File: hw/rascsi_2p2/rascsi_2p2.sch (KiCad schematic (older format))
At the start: 90 parts, among them IC1 SN74LS641-1DW, IC2 SN74LS641-1DW, IC3 SN74LS641-1DW, IC4 SN74LS641-1DW, J1 Raspberry_Pi_2_3, J2 Conn_01x02_Male, J3 Conn_02x25_Odd_Even, J4 I2C Pinout, J5 Conn_02x03_Odd_Even, J6 L717SDB25PA4CH4F, J7 Conn_01x02_Male, X1 Mac, X2 Dogcow, X3 Mac2, X4 Raspberry Pi, X5 Dogcow2, X6 Mac Trashcan, X7 Pi, X8 Pi

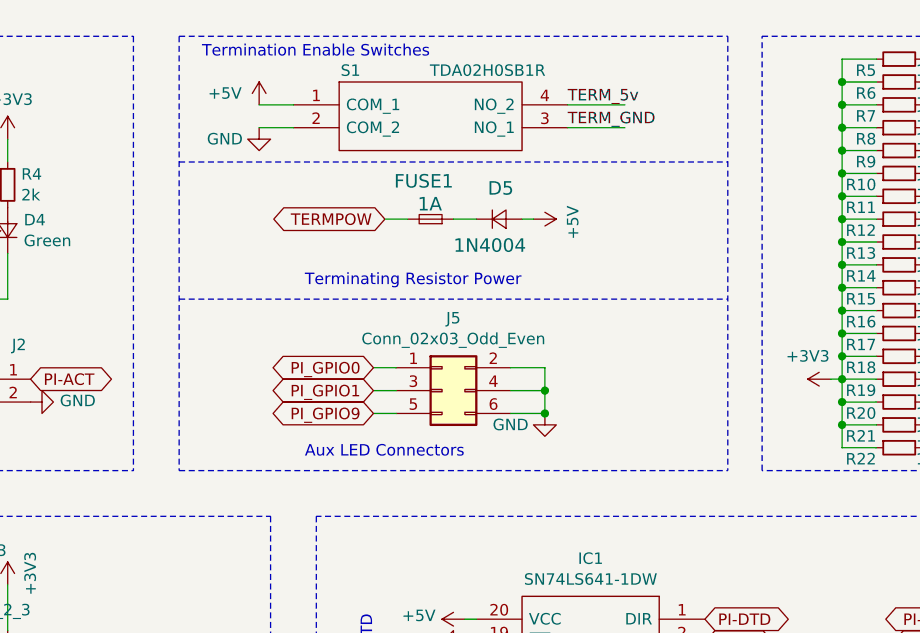
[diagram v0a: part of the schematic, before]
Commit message: Added USB port to power the raspberry pi. Labeled more pins on the silkscreen
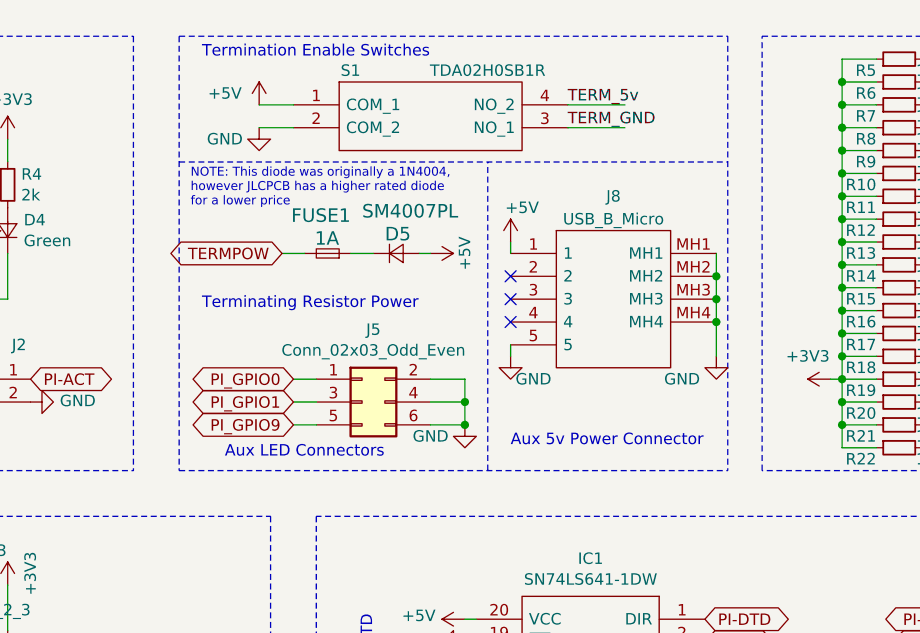
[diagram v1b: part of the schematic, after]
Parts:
- added J8: USB_B_Micro, SamacSys_Parts:U254051N4BH806, symbol SamacSys_Parts:U254-051N-4BH806
- D5: value 1N4004 -> SM4007PL; footprint Diode_SMD:D_SOD-123 -> Diode_SMD:D_SOD-123F; LCSC C162734 -> C64898
- J2: footprint Connector_PinHeader_2.54mm:PinHeader_1x02_P2.54mm_Vertical -> Connector_PinHeader_2.54mm:PinHeader_1x02_P2.54mm_Horizontal
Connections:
- net +5V: now also J8.1
- net GND: now also J8.5, J8.MH1, J8.MH2, J8.MH3, J8.MH4
- no-connect marks 2 -> 5
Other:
- note added: "Aux 5v Power Connector"
- note added: "NOTE: This diode was originally a 1N4004, \nhowever JLCPCB has a higher rated diode \nfor a lower price"
- moved on the sheet: D5, FUSE1, J5
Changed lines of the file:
@@
 L power:+5V #PWR021
 U 1 1 60874435
-P 4450 1350
-F 0 "#PWR021" H 4450 1200 50  0001 C CNN
-F 1 "+5V" H 4465 1523 50  0000 C CNN
-F 2 "" H 4450 1350 50  0001 C CNN
-F 3 "" H 4450 1350 50  0001 C CNN
-	1    4450 1350
+P 4000 1500
+F 0 "#PWR021" H 4000 1350 50  0001 C CNN
+F 1 "+5V" H 4000 1650 50  0000 C CNN
+F 2 "" H 4000 1500 50  0001 C CNN
+F 3 "" H 4000 1500 50  0001 C CNN
+	1    4000 1500
 	0    1    1    0
-$EndComp
-$Comp
-L Device:D_Small D5
-U 1 1 60874AD6
-P 4300 1350
-F 0 "D5" H 4250 1450 59  0000 L BNN
-F 1 "1N4004" H 4100 1200 59  0000 L BNN
-F 2 "Diode_SMD:D_SOD-123" H 4300 1350 50  0001 C CNN
-F 3 "" H 4300 1350 50  0001 C CNN
-F 4 "C162734" H 4300 1350 50  0001 C CNN "LCSC"
-	1    4300 1350
-	1    0    0    -1
 $EndComp
 $Comp
 L Device:Fuse_Small FUSE1
 U 1 1 60874FC5
-P 4000 1350
-F 0 "FUSE1" H 3900 1150 59  0000 L BNN
-F 1 "1A" H 3950 1250 59  0000 L BNN
-F 2 "Fuse:Fuse_1206_3216Metric" H 4000 1350 50  0001 C CNN
-F 3 "" H 4000 1350 50  0001 C CNN
-F 4 "C182974" H 4000 1350 50  0001 C CNN "LCSC"
-	1    4000 1350
+P 3550 1500
+F 0 "FUSE1" H 3450 1300 59  0000 L BNN
+F 1 "1A" H 3500 1400 59  0000 L BNN
+F 2 "Fuse:Fuse_1206_3216Metric" H 3550 1500 50  0001 C CNN
+F 3 "" H 3550 1500 50  0001 C CNN
+F 4 "C182974" H 3550 1500 50  0001 C CNN "LCSC"
+	1    3550 1500
 	-1   0    0    1
 $EndComp
 Wire Wire Line
-	4450 1350 4400 1350
+	4000 1500 3950 1500
 Text GLabel 6300 2250 2    50   BiDi ~ 0
 PI-D0
@@
 Wire Notes Line
 	8100 2650 3500 2650
-Text Notes 3450 1650 0    50   ~ 0
+Text Notes 3000 1750 0    50   ~ 0
 Terminating Resistor Power
 Text Notes 3550 6350 0    50   ~ 0
@@
 Wire Wire Line
 	8950 2150 8500 2150
-Text GLabel 3800 1350 0    50   BiDi ~ 0
+Text GLabel 3350 1500 0    50   BiDi ~ 0
 TERMPOW
 $Comp
@@
 F 0 "J2" H 2200 2200 50  0000 C CNN
 F 1 "Conn_01x02_Male" H 2158 2140 50  0001 C CNN
-F 2 "Connector_PinHeader_2.54mm:PinHeader_1x02_P2.54mm_Vertical" H 2050 2050 50  0001 C CNN
+F 2 "Connector_PinHeader_2.54mm:PinHeader_1x02_P2.54mm_Horizontal" H 2050 2050 50  0001 C CNN
 F 3 "~" H 2050 2050 50  0001 C CNN
 	1    2050 2050
@@
 	5750 2050 5800 2050
 Wire Wire Line
-	4200 1350 4100 1350
-Wire Wire Line
-	3900 1350 3800 1350
+	3750 1500 3650 1500
+Wire Wire Line
+	3450 1500 3350 1500
 $Comp
 L SamacSys_Parts:Logo X8
@@
 Text GLabel 2750 3650 2    50   BiDi ~ 0
 PI_GPIO1
-Text GLabel 3750 2000 0    50   BiDi ~ 0
+Text GLabel 3400 2050 0    50   BiDi ~ 0
 PI_GPIO0
-Text GLabel 3750 2100 0    50   BiDi ~ 0
+Text GLabel 3400 2150 0    50   BiDi ~ 0
 PI_GPIO1
 Text GLabel 2750 4750 2    50   BiDi ~ 0
 PI_GPIO9
-Text GLabel 3750 2200 0    50   BiDi ~ 0
+Text GLabel 3400 2250 0    50   BiDi ~ 0
 PI_GPIO9
 Connection ~ 1200 1700
@@
 L Connector_Generic:Conn_02x03_Odd_Even J5
 U 1 1 5F604F7F
-P 4050 2100
-F 0 "J5" H 4100 2417 50  0000 C CNN
-F 1 "Conn_02x03_Odd_Even" H 4100 2326 50  0000 C CNN
-F 2 "Connector_PinHeader_2.54mm:PinHeader_2x03_P2.54mm_Vertical" H 4050 2100 50  0001 C CNN
-F 3 "~" H 4050 2100 50  0001 C CNN
-	1    4050 2100
-	1    0    0    -1
-$EndComp
-Wire Wire Line
-	3750 2000 3850 2000
-Wire Wire Line
-	3750 2100 3850 2100
-Wire Wire Line
-	3750 2200 3850 2200
+P 3700 2150
+F 0 "J5" H 3750 2467 50  0000 C CNN
+F 1 "Conn_02x03_Odd_Even" H 3750 2376 50  0000 C CNN
+F 2 "Connector_PinHeader_2.54mm:PinHeader_2x03_P2.54mm_Vertical" H 3700 2150 50  0001 C CNN
+F 3 "~" H 3700 2150 50  0001 C CNN
+	1    3700 2150
+	1    0    0    -1
+$EndComp
+Wire Wire Line
+	3400 2050 3500 2050
+Wire Wire Line
+	3400 2150 3500 2150
+Wire Wire Line
+	3400 2250 3500 2250
 $Comp
 L power:GND #PWR022
 U 1 1 5F648FEB
-P 4500 2200
-F 0 "#PWR022" H 4500 1950 50  0001 C CNN
-F 1 "GND" H 4350 2150 50  0000 C CNN
-F 2 "" H 4500 2200 50  0001 C CNN
-F 3 "" H 4500 2200 50  0001 C CNN
-	1    4500 2200
-	1    0    0    -1
-$EndComp
-Wire Wire Line
-	4500 2200 4500 2100
-Wire Wire Line
-	4500 2000 4350 2000
-Wire Wire Line
-	4350 2100 4500 2100
-Connection ~ 4500 2100
-Wire Wire Line
-	4500 2100 4500 2000
-Wire Wire Line
-	4350 2200 4500 2200
-Connection ~ 4500 2200
-Wire Notes Line
-	2900 1700 5300 1700
-Text Notes 3450 2400 0    50   ~ 0
+P 4150 2250
+F 0 "#PWR022" H 4150 2000 50  0001 C CNN
+F 1 "GND" H 4000 2200 50  0000 C CNN
+F 2 "" H 4150 2250 50  0001 C CNN
+F 3 "" H 4150 2250 50  0001 C CNN
+	1    4150 2250
+	1    0    0    -1
+$EndComp
+Wire Wire Line
+	4150 2250 4150 2150
+Wire Wire Line
+	4150 2050 4000 2050
+Wire Wire Line
+	4000 2150 4150 2150
+Connection ~ 4150 2150
+Wire Wire Line
+	4150 2150 4150 2050
+Wire Wire Line
+	4000 2250 4150 2250
+Connection ~ 4150 2250
+Text Notes 3100 2400 0    50   ~ 0
 Aux LED Connectors
 $Comp
@@
 Text GLabel 2100 7050 1    50   BiDi ~ 0
 TERMPOW
+$Comp
+L SamacSys_Parts:U254-051N-4BH806 J8
+U 1 1 5F3EF01D
+P 4350 1500
+F 0 "J8" H 4800 1750 50  0000 C CNN
+F 1 "USB_B_Micro" H 4800 1650 50  0000 C CNN
+F 2 "SamacSys_Parts:U254051N4BH806" H 4500 1450 50  0001 C CNN
+F 3 "~" H 4500 1450 50  0001 C CNN
+	1    4350 1500
+	1    0    0    -1
+$EndComp
+$Comp
+L power:GND #PWR050
+U 1 1 5F3F2094
+P 4350 1950
+F 0 "#PWR050" H 4350 1700 50  0001 C CNN
+F 1 "GND" H 4450 1850 50  0000 C CNN
+F 2 "" H 4350 1950 50  0001 C CNN
+F 3 "" H 4350 1950 50  0001 C CNN
+	1    4350 1950
+	1    0    0    -1
+$EndComp
+$Comp
+L power:GND #PWR051
+U 1 1 5F3F244A
+P 5250 1950
+F 0 "#PWR051" H 5250 1700 50  0001 C CNN
+F 1 "GND" H 5100 1850 50  0000 C CNN
+F 2 "" H 5250 1950 50  0001 C CNN
+F 3 "" H 5250 1950 50  0001 C CNN
+	1    5250 1950
+	1    0    0    -1
+$EndComp
+$Comp
+L power:+5V #PWR052
+U 1 1 5F3F254A
+P 4350 1450
+F 0 "#PWR052" H 4350 1300 50  0001 C CNN
+F 1 "+5V" H 4400 1600 50  0000 C CNN
+F 2 "" H 4350 1450 50  0001 C CNN
+F 3 "" H 4350 1450 50  0001 C CNN
+	1    4350 1450
+	1    0    0    -1
+$EndComp
+NoConn ~ 4350 1600
+NoConn ~ 4350 1700
+NoConn ~ 4350 1800
+Wire Notes Line
+	4250 2450 4250 1100
+Text Notes 4350 2350 0    50   ~ 0
+Aux 5v Power Connector
+Connection ~ 5250 1600
+Wire Wire Line
+	5250 1600 5250 1500
+Connection ~ 5250 1700
+Wire Wire Line
+	5250 1700 5250 1600
+Connection ~ 5250 1800
+Wire Wire Line
+	5250 1800 5250 1700
+Wire Wire Line
+	4350 1500 4350 1450
+Wire Wire Line
+	4350 1900 4350 1950
+Wire Wire Line
+	5250 1800 5250 1950
+$Comp
+L Device:D_Small D5
+U 1 1 60874AD6
+P 3850 1500
+F 0 "D5" H 3800 1550 59  0000 L BNN
+F 1 "SM4007PL" H 3700 1650 59  0000 L BNN
+F 2 "Diode_SMD:D_SOD-123F" H 3850 1500 50  0001 C CNN
+F 3 "" H 3850 1500 50  0001 C CNN
+F 4 "C64898" H 3850 1500 50  0001 C CNN "LCSC"
+	1    3850 1500
+	1    0    0    -1
+$EndComp
+Text Notes 2950 1300 0    39   ~ 0
+NOTE: This diode was originally a 1N4004, \nhowever JLCPCB has a higher rated diode \nfor a lower price
 $EndSCHEMATC

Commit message: Added LCSC part number for USB connector
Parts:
- J8: LCSC (none) -> C319170
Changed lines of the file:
@@
 F 2 "SamacSys_Parts:U254051N4BH806" H 4500 1450 50  0001 C CNN
 F 3 "~" H 4500 1450 50  0001 C CNN
+F 4 "C319170" H 4350 1500 50  0001 C CNN "LCSC"
 	1    4350 1500
 	1    0    0    -1

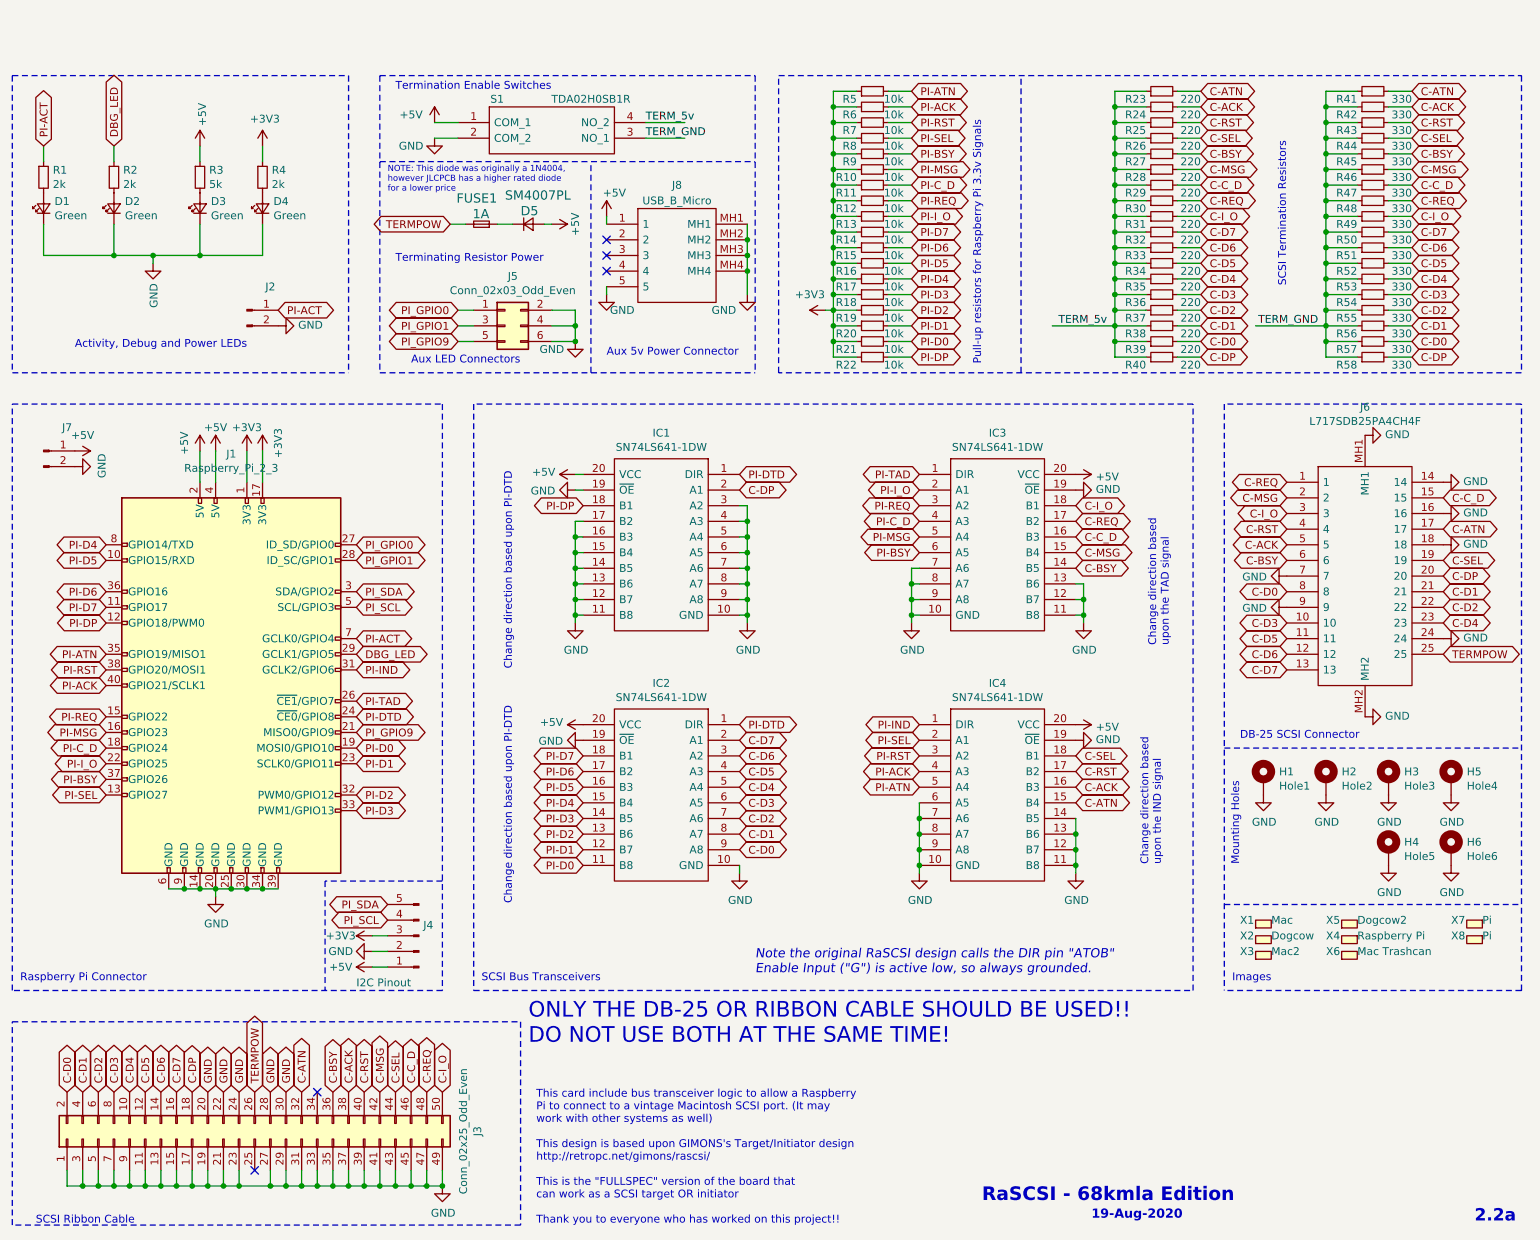
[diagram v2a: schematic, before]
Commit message: Cleanup LCSC part number, regenerate gerbers and re-generate schematics
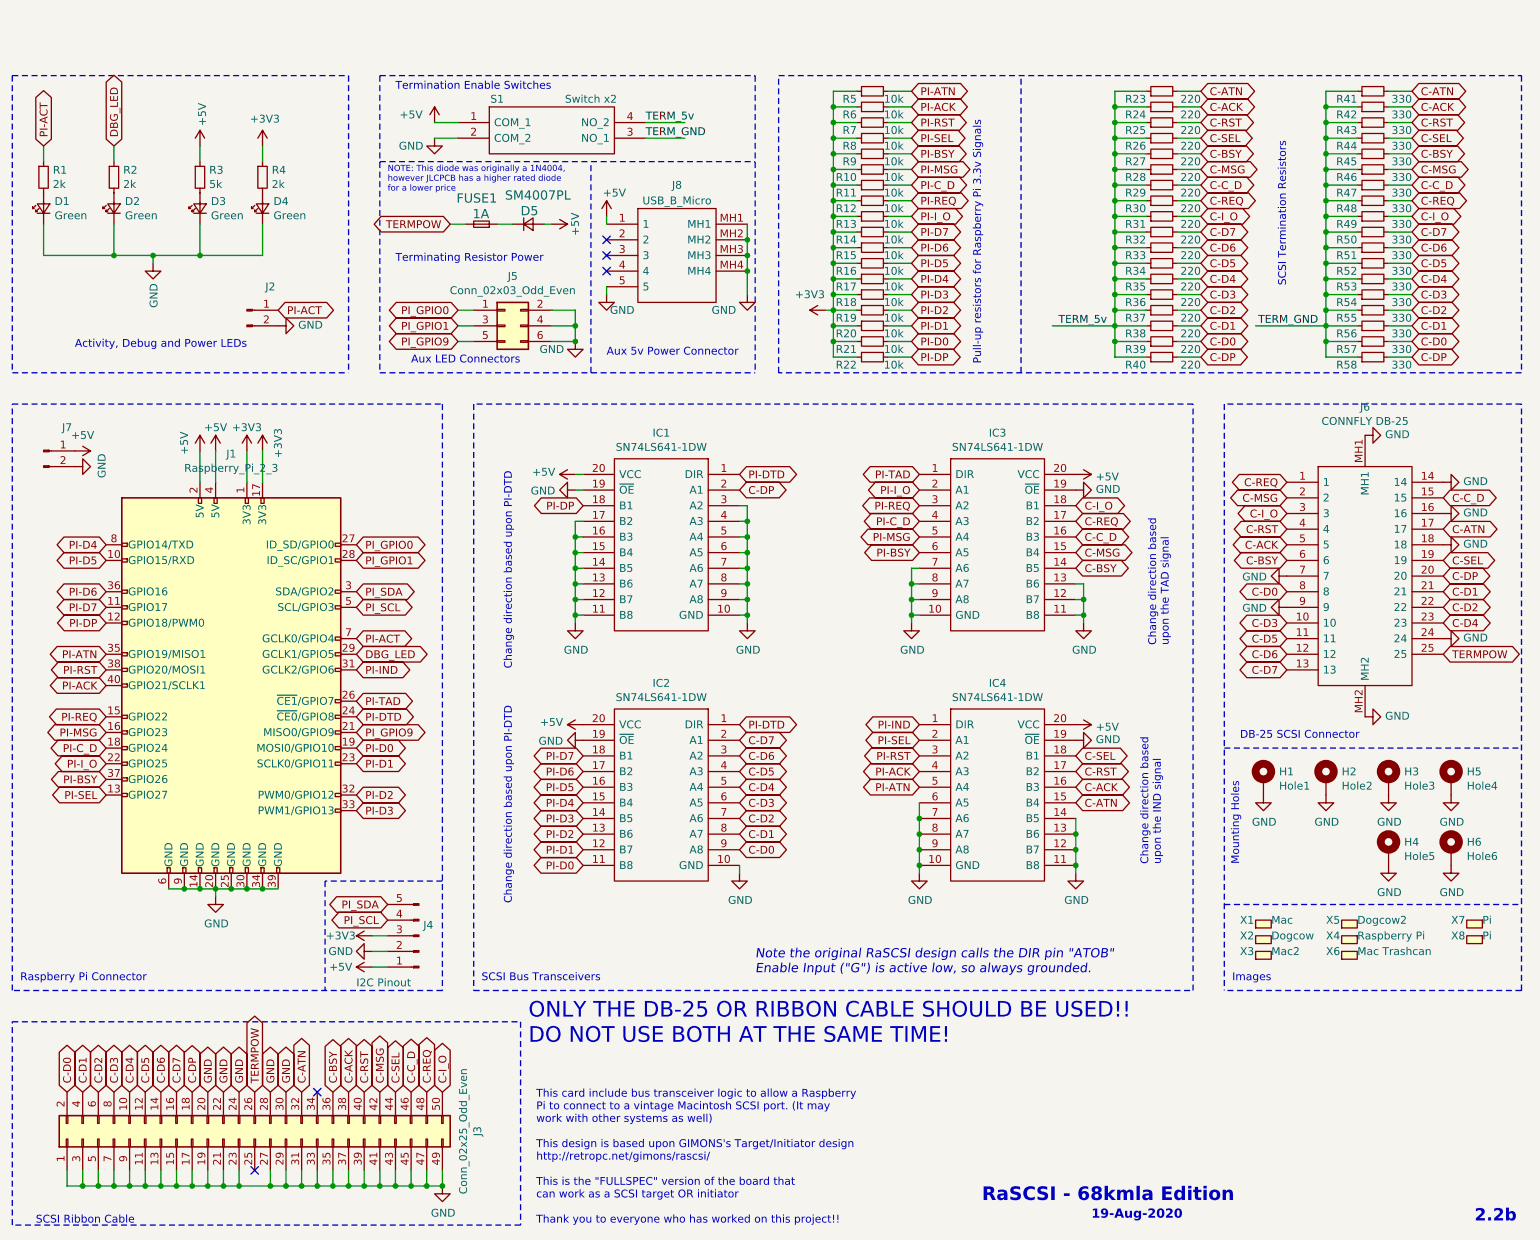
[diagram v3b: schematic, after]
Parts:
- J1: LCSC (none) -> C50982
- J2, J4, J7: LCSC (none) -> C2337
- J3: LCSC (none) -> C30006
- J5: LCSC (none) -> C3409
- J6: value L717SDB25PA4CH4F -> CONNFLY DB-25; LCSC (none) -> C77838
- S1: value TDA02H0SB1R -> Switch x2; LCSC (none) -> C40735
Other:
- note added: "2.2b"
- note removed: "2.2a"
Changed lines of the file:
@@
 F 2 "Connector_PinHeader_2.54mm:PinHeader_2x25_P2.54mm_Vertical" H 2100 7350 50  0001 C CNN
 F 3 "~" H 2100 7350 50  0001 C CNN
+F 4 "C30006" H 2100 7350 50  0001 C CNN "LCSC"
 	1    2100 7350
 	0    -1   -1   0
@@
 F 2 "Connector_PinSocket_2.54mm:PinSocket_2x20_P2.54mm_Vertical" H 1950 4450 50  0001 C CNN
 F 3 "https://www.raspberrypi.org/documentation/hardware/raspberrypi/schematics/rpi_SCH_3bplus_1p0_reduced.pdf" H 1950 4450 50  0001 C CNN
+F 4 "C50982" H 1950 4450 50  0001 C CNN "LCSC"
 	1    1950 4450
 	1    0    0    -1
@@
 F 2 "Connector_PinSocket_2.54mm:PinSocket_1x05_P2.54mm_Vertical" H 3150 6050 50  0001 C CNN
 F 3 "~" H 3150 6050 50  0001 C CNN
+F 4 "C2337" H 3150 6050 50  0001 C CNN "LCSC"
 	1    3150 6050
 	-1   0    0    1
@@
 P 3400 850
 F 0 "S1" H 3650 1000 50  0000 C CNN
-F 1 "TDA02H0SB1R" H 4250 1000 50  0000 C CNN
+F 1 "Switch x2" H 4250 1000 50  0000 C CNN
 F 2 "rascsi_din:SOIC127P812X230-4N" H 4450 950 50  0001 L CNN
 F 3 "https://www.ckswitches.com/media/1328/tda.pdf" H 4450 850 50  0001 L CNN
@@
 F 8 "C & K COMPONENTS" H 4450 350 50  0001 L CNN "Manufacturer_Name"
 F 9 "TDA02H0SB1R" H 4450 250 50  0001 L CNN "Manufacturer_Part_Number"
+F 10 "C40735" H 3400 850 50  0001 C CNN "LCSC"
 	1    3400 850
 	1    0    0    -1
@@
 F 2 "Connector_PinHeader_2.54mm:PinHeader_1x02_P2.54mm_Horizontal" H 2050 2050 50  0001 C CNN
 F 3 "~" H 2050 2050 50  0001 C CNN
+F 4 "C2337" H 2050 2050 50  0001 C CNN "LCSC"
 	1    2050 2050
 	1    0    0    -1
@@
 P 9200 2850
 F 0 "J6" V 9019 2850 50  0000 C CNN
-F 1 "L717SDB25PA4CH4F" V 9110 2850 50  0000 C CNN
+F 1 "CONNFLY DB-25" V 9110 2850 50  0000 C CNN
 F 2 "L717SDB25PA4CH4F" H 10850 3150 50  0001 L CNN
 F 3 "https://componentsearchengine.com/Datasheets/1/L717SDB25PA4CH4F.pdf" H 10850 3050 50  0001 L CNN
@@
 F 8 "Amphenol" H 10850 2550 50  0001 L CNN "Manufacturer_Name"
 F 9 "L717SDB25PA4CH4F" H 10850 2450 50  0001 L CNN "Manufacturer_Part_Number"
+F 10 "C77838" V 9200 2850 50  0001 C CNN "LCSC"
 	1    9200 2850
 	0    -1   1    0
@@
 RaSCSI - 68kmla Edition
 Text Notes 9900 7890 0    79   ~ 16
-2.2a
+2.2b
 Text Notes 7450 7870 0    59   ~ 12
 19-Aug-2020
@@
 F 2 "Connector_PinHeader_2.54mm:PinHeader_2x03_P2.54mm_Vertical" H 3700 2150 50  0001 C CNN
 F 3 "~" H 3700 2150 50  0001 C CNN
+F 4 "C3409" H 3700 2150 50  0001 C CNN "LCSC"
 	1    3700 2150
 	1    0    0    -1
@@
 F 2 "Connector_PinHeader_2.54mm:PinHeader_1x02_P2.54mm_Vertical" H 750 2950 50  0001 C CNN
 F 3 "~" H 750 2950 50  0001 C CNN
+F 4 "C2337" H 750 2950 50  0001 C CNN "LCSC"
 	1    750  2950
 	1    0    0    -1
